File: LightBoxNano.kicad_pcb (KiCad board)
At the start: 2 copper layers, 59 parts, among them J5V1 Conn_02 DNP, SW1 Knitter-Switch DRR4010

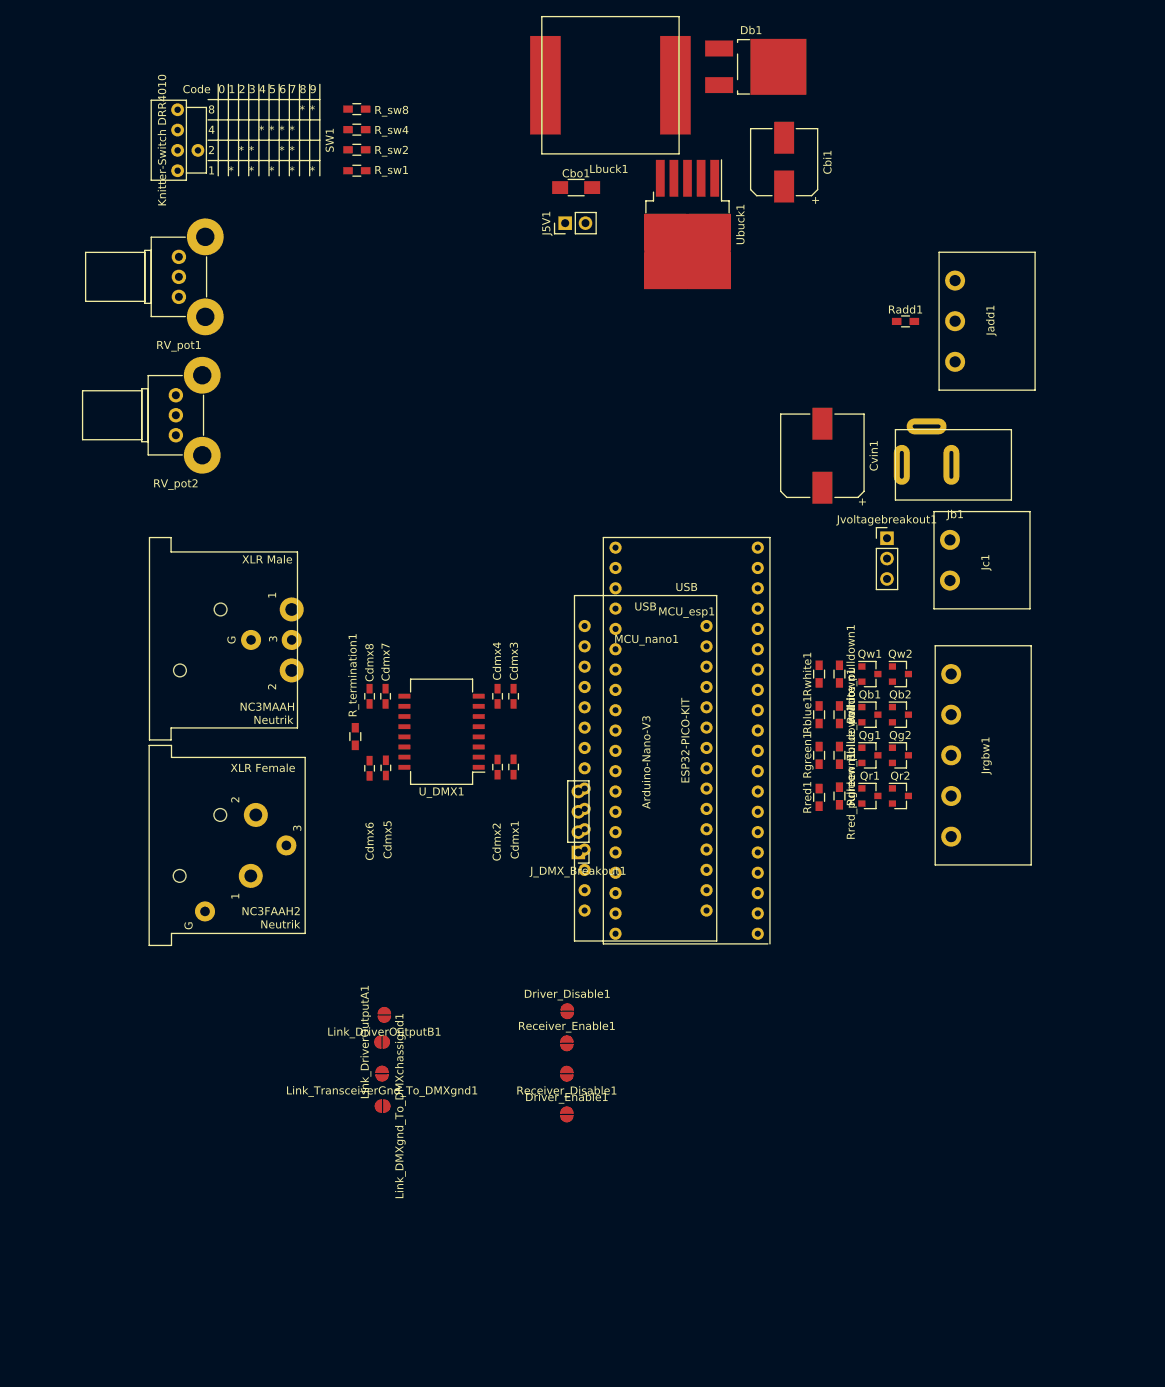
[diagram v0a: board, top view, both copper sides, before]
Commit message: Nicer placment of labels and components on PCB
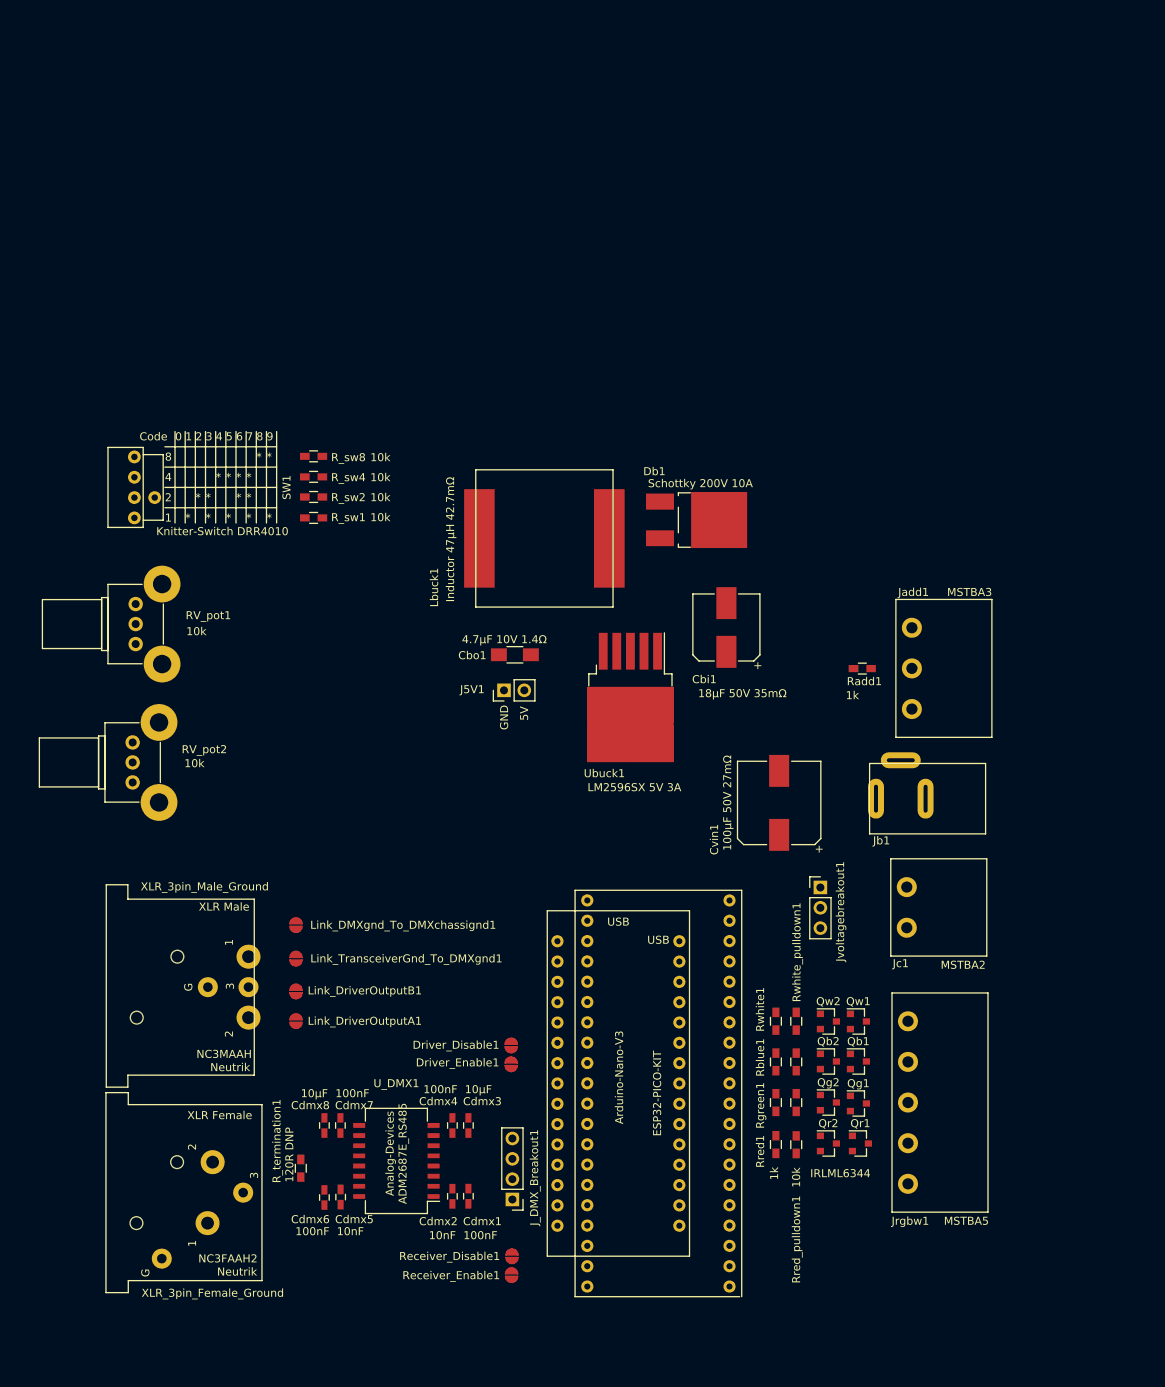
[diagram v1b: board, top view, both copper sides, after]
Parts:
- moved Ubuck1 59.6 mm to (159.6, 67.2)
- moved Cbo1 58.9 mm to (145.2, 61.8)
- moved J5V1 58.9 mm to (143.8, 66.3)
- moved Cbi1 58.6 mm to (171.6, 58.4)
- moved Lbuck1 57.2 mm to (148.8, 47.3)
- moved Db1 57.1 mm to (167.9, 45.0)
- moved R_termination1 54.4 mm to (118.4, 126.0)
- moved Cdmx1 53.9 mm to (139.3, 129.5), turned to 90 degrees
- moved Cdmx3 53.9 mm to (139.3, 120.7), turned to 90 degrees
- moved Cdmx4 53.9 mm to (137.3, 120.7)
- moved Cdmx6 53.9 mm to (121.3, 129.7)
- moved Cdmx7 53.9 mm to (123.3, 120.7)
- moved Cdmx8 53.9 mm to (121.3, 120.7)
- moved U_DMX1 53.9 mm to (130.3, 125.1)
- moved Cdmx2 53.9 mm to (137.3, 129.5)
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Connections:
- J5V1 pad 1: +5V -> GND
- J5V1 pad 2: GND -> +5V
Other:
- board text added: "Analog-Devices ADM2687E_RS485"

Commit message: Add 3mm mounting holes
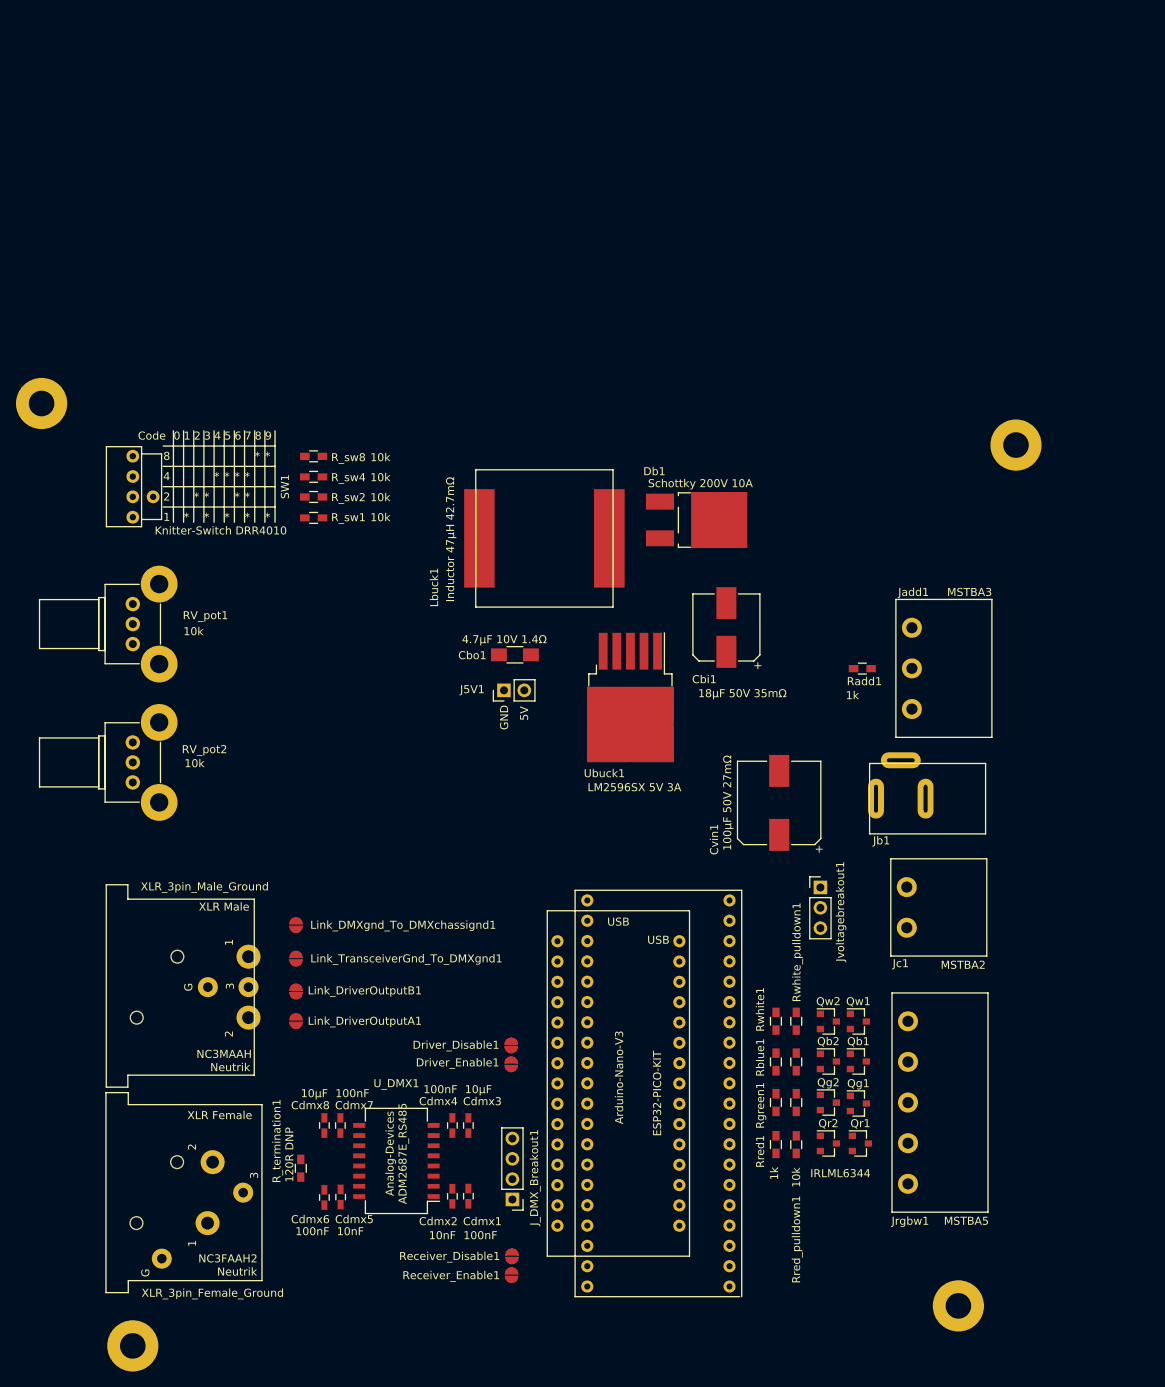
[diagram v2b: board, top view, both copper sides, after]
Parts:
- added H1: MountingHole, Mounting_Holes:MountingHole_3.2mm_M3_Pad, F.Cu at (86.0, 30.4)
- added H2: MountingHole, Mounting_Holes:MountingHole_3.2mm_M3_Pad, F.Cu at (97.4, 148.2)
- added H3: MountingHole, Mounting_Holes:MountingHole_3.2mm_M3_Pad, F.Cu at (207.8, 35.6)
- added H4: MountingHole, Mounting_Holes:MountingHole_3.2mm_M3_Pad, F.Cu at (200.6, 143.2)
- moved RV_pot1 0.36 mm to (97.4, 55.5)
- moved SW1 0.22 mm to (97.4, 40.8)
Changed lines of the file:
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@@
     (tracks 0)
     (zones 0)
-    (modules 59)
+    (modules 63)
     (nets 73)
   )
@@
     (add_net "Net-(Ubuck1-Pad5)")
   )
+  (module Mounting_Holes:MountingHole_3.2mm_M3_Pad (layer F.Cu)
+    (at 200.6 143.2)
+    (descr "Mounting Hole 3.2mm, M3")
+    (tags "mounting hole 3.2mm m3")
+    (attr virtual)
+    (fp_text reference H4 (at 0 -4.2) (layer F.SilkS) hide
+      (effects (font (size 1 1) (thickness 0.15)))
+    )
+    (fp_text value MountingHole (at 0 4.2) (layer F.Fab) hide
+      (effects (font (size 1 1) (thickness 0.15)))
+    )
+    (fp_circle (center 0 0) (end 3.2 0) (layer Cmts.User) (width 0.15))
+    (fp_circle (center 0 0) (end 3.45 0) (layer F.CrtYd) (width 0.05))
+    (pad 1 thru_hole circle (at 0 0) (size 6.4 6.4) (drill 3.2) (layers *.Cu *.Mask))
+  )
+  (module Mounting_Holes:MountingHole_3.2mm_M3_Pad (layer F.Cu)
+    (at 207.8 35.6)
+    (descr "Mounting Hole 3.2mm, M3")
+    (tags "mounting hole 3.2mm m3")
+    (attr virtual)
+    (fp_text reference H3 (at 0 -4.2) (layer F.SilkS) hide
+      (effects (font (size 1 1) (thickness 0.15)))
+    )
+    (fp_text value MountingHole (at 0 4.2) (layer F.Fab) hide
+      (effects (font (size 1 1) (thickness 0.15)))
+    )
+    (fp_circle (center 0 0) (end 3.2 0) (layer Cmts.User) (width 0.15))
+    (fp_circle (center 0 0) (end 3.45 0) (layer F.CrtYd) (width 0.05))
+    (pad 1 thru_hole circle (at 0 0) (size 6.4 6.4) (drill 3.2) (layers *.Cu *.Mask))
+  )
+  (module Mounting_Holes:MountingHole_3.2mm_M3_Pad (layer F.Cu)
+    (at 97.4 148.2)
+    (descr "Mounting Hole 3.2mm, M3")
+    (tags "mounting hole 3.2mm m3")
+    (attr virtual)
+    (fp_text reference H2 (at 0 -4.2) (layer F.SilkS) hide
+      (effects (font (size 1 1) (thickness 0.15)))
+    )
+    (fp_text value MountingHole (at 0 4.2) (layer F.Fab) hide
+      (effects (font (size 1 1) (thickness 0.15)))
+    )
+    (fp_circle (center 0 0) (end 3.2 0) (layer Cmts.User) (width 0.15))
+    (fp_circle (center 0 0) (end 3.45 0) (layer F.CrtYd) (width 0.05))
+    (pad 1 thru_hole circle (at 0 0) (size 6.4 6.4) (drill 3.2) (layers *.Cu *.Mask))
+  )
+  (module Mounting_Holes:MountingHole_3.2mm_M3_Pad (layer F.Cu)
+    (at 86 30.4)
+    (descr "Mounting Hole 3.2mm, M3")
+    (tags "mounting hole 3.2mm m3")
+    (attr virtual)
+    (fp_text reference H1 (at 0 -4.2) (layer F.SilkS) hide
+      (effects (font (size 1 1) (thickness 0.15)))
+    )
+    (fp_text value MountingHole (at 0 4.2) (layer F.Fab) hide
+      (effects (font (size 1 1) (thickness 0.15)))
+    )
+    (fp_circle (center 0 0) (end 3.2 0) (layer Cmts.User) (width 0.15))
+    (fp_circle (center 0 0) (end 3.45 0) (layer F.CrtYd) (width 0.05))
+    (pad 1 thru_hole circle (at 0 0) (size 6.4 6.4) (drill 3.2) (layers *.Cu *.Mask))
+  )
   (module Capacitors_SMD:C_0603_HandSoldering (layer F.Cu)
     (at 121.35 120.65 90)
@@
   )
   (module Potentiometers:Potentiometer_Alps_RK09K_Vertical (layer F.Cu)
-    (at 97.7621 55.47262 180)
+    (at 97.4 55.47262 180)
     (descr "Potentiometer, vertically mounted, Omeg PC16PU, Omeg PC16PU, Omeg PC16PU, Vishay/Spectrol 248GJ/249GJ Single, Vishay/Spectrol 248GJ/249GJ Single, Vishay/Spectrol 248GJ/249GJ Single, Vishay/Spectrol 248GH/249GH Single, Vishay/Spectrol 148/149 Single, Vishay/Spectrol 148/149 Single, Vishay/Spectrol 148/149 Single, Vishay/Spectrol 148A/149A Single with mounting plates, Vishay/Spectrol 148/149 Double, Vishay/Spectrol 148A/149A Double with mounting plates, Piher PC-16 Single, Piher PC-16 Single, Piher PC-16 Single, Piher PC-16SV Single, Piher PC-16 Double, Piher PC-16 Triple, Piher T16H Single, Piher T16L Single, Piher T16H Double, Alps RK163 Single, Alps RK163 Double, Alps RK097 Single, Alps RK097 Double, Bourns PTV09A-2 Single with mounting sleve Single, Bourns PTV09A-1 with mounting sleve Single, Bourns PRS11S Single, Alps RK09K Single with mounting sleve Single, http://www.alps.com/prod/info/E/HTML/Potentiometer/RotaryPotentiometers/RK09K/RK09K1110A2S.html")
     (tags "Potentiometer vertical  Omeg PC16PU  Omeg PC16PU  Omeg PC16PU  Vishay/Spectrol 248GJ/249GJ Single  Vishay/Spectrol 248GJ/249GJ Single  Vishay/Spectrol 248GJ/249GJ Single  Vishay/Spectrol 248GH/249GH Single  Vishay/Spectrol 148/149 Single  Vishay/Spectrol 148/149 Single  Vishay/Spectrol 148/149 Single  Vishay/Spectrol 148A/149A Single with mounting plates  Vishay/Spectrol 148/149 Double  Vishay/Spectrol 148A/149A Double with mounting plates  Piher PC-16 Single  Piher PC-16 Single  Piher PC-16 Single  Piher PC-16SV Single  Piher PC-16 Double  Piher PC-16 Triple  Piher T16H Single  Piher T16L Single  Piher T16H Double  Alps RK163 Single  Alps RK163 Double  Alps RK097 Single  Alps RK097 Double  Bourns PTV09A-2 Single with mounting sleve Single  Bourns PTV09A-1 with mounting sleve Single  Bourns PRS11S Single  Alps RK09K Single with mounting sleve Single")
@@
   )
   (module Potentiometers:Potentiometer_Alps_RK09K_Vertical (layer F.Cu)
-    (at 97.3811 72.77002 180)
+    (at 97.4 72.77002 180)
     (descr "Potentiometer, vertically mounted, Omeg PC16PU, Omeg PC16PU, Omeg PC16PU, Vishay/Spectrol 248GJ/249GJ Single, Vishay/Spectrol 248GJ/249GJ Single, Vishay/Spectrol 248GJ/249GJ Single, Vishay/Spectrol 248GH/249GH Single, Vishay/Spectrol 148/149 Single, Vishay/Spectrol 148/149 Single, Vishay/Spectrol 148/149 Single, Vishay/Spectrol 148A/149A Single with mounting plates, Vishay/Spectrol 148/149 Double, Vishay/Spectrol 148A/149A Double with mounting plates, Piher PC-16 Single, Piher PC-16 Single, Piher PC-16 Single, Piher PC-16SV Single, Piher PC-16 Double, Piher PC-16 Triple, Piher T16H Single, Piher T16L Single, Piher T16H Double, Alps RK163 Single, Alps RK163 Double, Alps RK097 Single, Alps RK097 Double, Bourns PTV09A-2 Single with mounting sleve Single, Bourns PTV09A-1 with mounting sleve Single, Bourns PRS11S Single, Alps RK09K Single with mounting sleve Single, http://www.alps.com/prod/info/E/HTML/Potentiometer/RotaryPotentiometers/RK09K/RK09K1110A2S.html")
     (tags "Potentiometer vertical  Omeg PC16PU  Omeg PC16PU  Omeg PC16PU  Vishay/Spectrol 248GJ/249GJ Single  Vishay/Spectrol 248GJ/249GJ Single  Vishay/Spectrol 248GJ/249GJ Single  Vishay/Spectrol 248GH/249GH Single  Vishay/Spectrol 148/149 Single  Vishay/Spectrol 148/149 Single  Vishay/Spectrol 148/149 Single  Vishay/Spectrol 148A/149A Single with mounting plates  Vishay/Spectrol 148/149 Double  Vishay/Spectrol 148A/149A Double with mounting plates  Piher PC-16 Single  Piher PC-16 Single  Piher PC-16 Single  Piher PC-16SV Single  Piher PC-16 Double  Piher PC-16 Triple  Piher T16H Single  Piher T16L Single  Piher T16H Double  Alps RK163 Single  Alps RK163 Double  Alps RK097 Single  Alps RK097 Double  Bourns PTV09A-2 Single with mounting sleve Single  Bourns PTV09A-1 with mounting sleve Single  Bourns PRS11S Single  Alps RK09K Single with mounting sleve Single")
@@
   )
   (module Knitter-Switch:DRR4010 (layer F.Cu)
-    (at 97.6 40.89302 90)
+    (at 97.4 40.8 90)
     (fp_text reference SW1 (at 0 19.05 90) (layer F.SilkS)
       (effects (font (size 1 1) (thickness 0.15)))
